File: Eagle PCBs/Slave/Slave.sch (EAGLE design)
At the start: 7 parts, among them Q1 TIP120

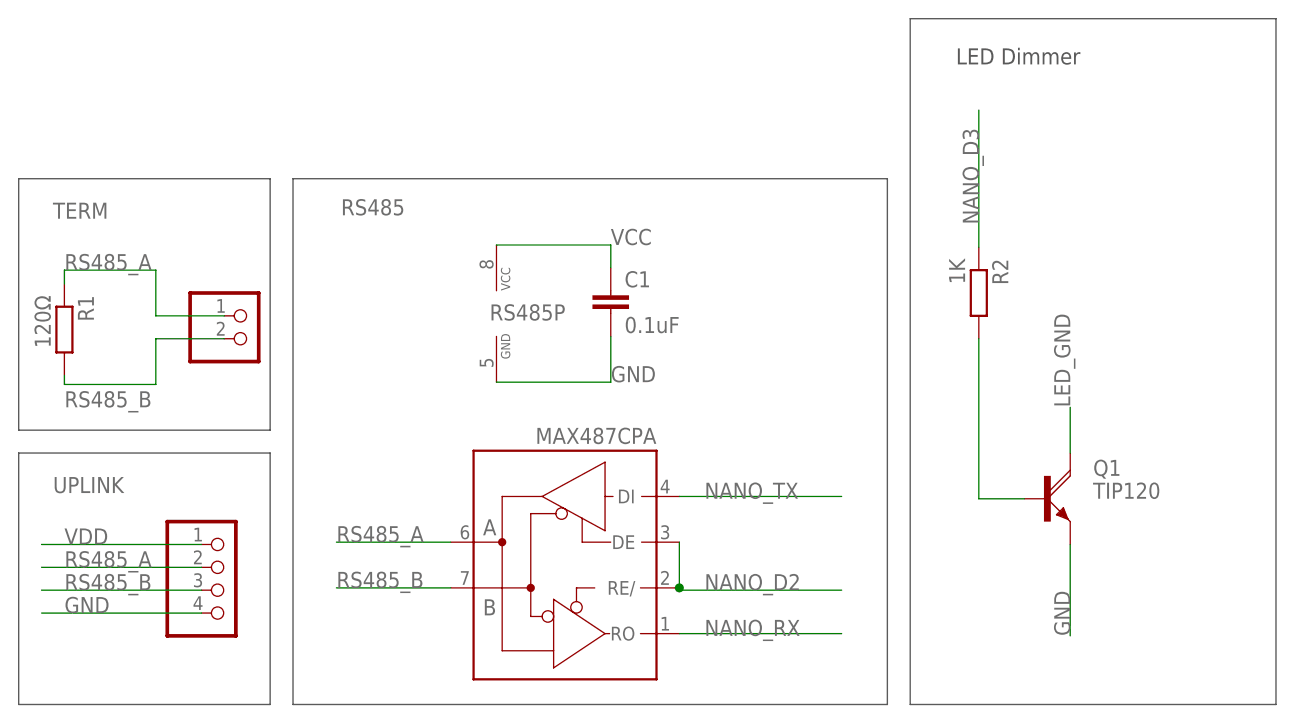
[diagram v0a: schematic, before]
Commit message: Added LED circuit to Slave PCB
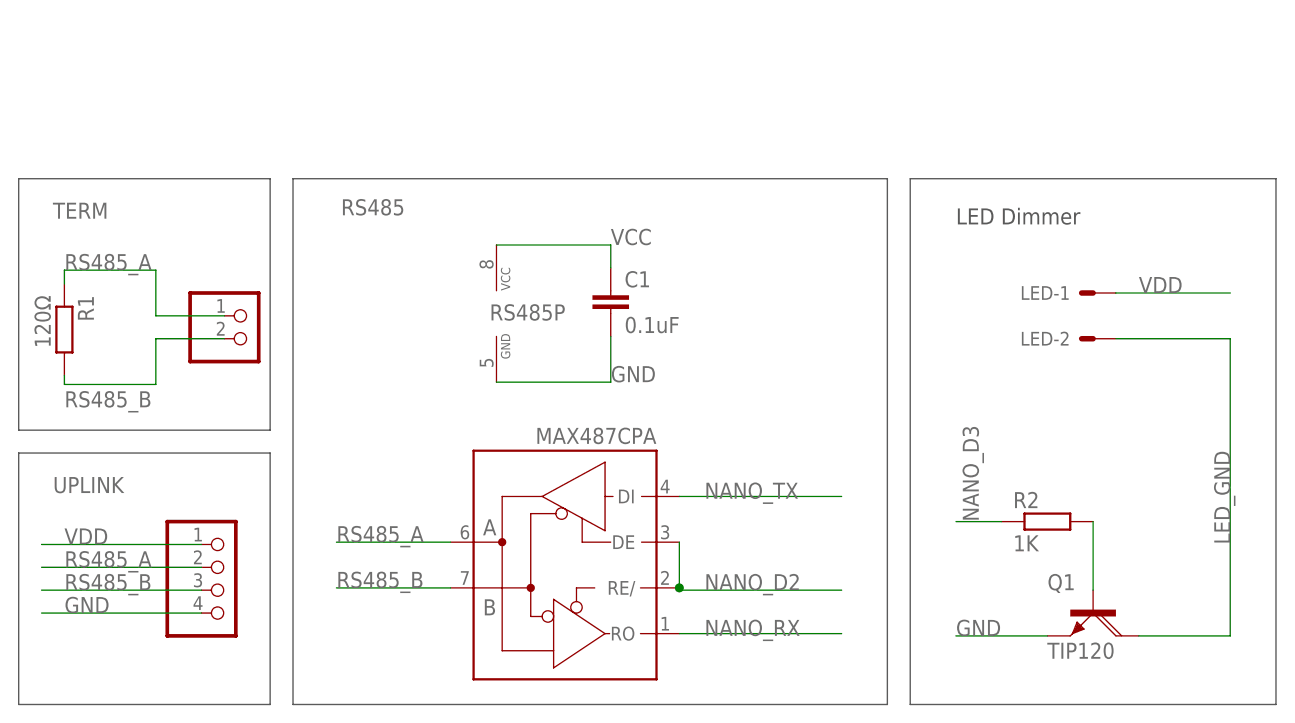
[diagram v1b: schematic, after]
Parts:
- added LED: (no value), con-molex:KK-156-2
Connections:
- net LED_GND: now also LED-2.S
- net VDD: now also LED-1.S
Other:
- moved on the sheet: Q1, R2
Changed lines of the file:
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@@
 <part name="Q1" library="transistor-power" library_urn="urn:adsk.eagle:library:400" deviceset="TIP120" device="" package3d_urn="urn:adsk.eagle:package:29488/1"/>
 <part name="UPLINK" library="pinhead" library_urn="urn:adsk.eagle:library:325" deviceset="PINHD-1X4" device="" package3d_urn="urn:adsk.eagle:package:22407/2"/>
+<part name="LED" library="con-molex" library_urn="urn:adsk.eagle:library:165" deviceset="KK-156-2" device="" package3d_urn="urn:adsk.eagle:package:8078800/1"/>
 </parts>
 <sheets>
 <sheet>
 <plain>
-<text x="106.68" y="73.66" size="1.778" layer="97">LED Dimmer</text>
-<wire x1="101.6" y1="78.74" x2="142.24" y2="78.74" width="0.1524" layer="97"/>
-<wire x1="142.24" y1="78.74" x2="142.24" y2="2.54" width="0.1524" layer="97"/>
+<text x="106.68" y="55.88" size="1.778" layer="97">LED Dimmer</text>
+<wire x1="101.6" y1="60.96" x2="142.24" y2="60.96" width="0.1524" layer="97"/>
+<wire x1="142.24" y1="60.96" x2="142.24" y2="2.54" width="0.1524" layer="97"/>
 <wire x1="142.24" y1="2.54" x2="101.6" y2="2.54" width="0.1524" layer="97"/>
-<wire x1="101.6" y1="2.54" x2="101.6" y2="78.74" width="0.1524" layer="97"/>
+<wire x1="101.6" y1="2.54" x2="101.6" y2="60.96" width="0.1524" layer="97"/>
 <wire x1="2.54" y1="2.54" x2="2.54" y2="30.48" width="0.1524" layer="97"/>
 <wire x1="2.54" y1="30.48" x2="30.48" y2="30.48" width="0.1524" layer="97"/>
@@
 <attribute name="VALUE" x="4.318" y="48.006" size="1.778" layer="96" rot="R270"/>
 </instance>
-<instance part="R2" gate="G$1" x="109.22" y="48.26" smashed="yes" rot="R270">
-<attribute name="NAME" x="110.7186" y="52.07" size="1.778" layer="95" rot="R270"/>
-<attribute name="VALUE" x="105.918" y="52.07" size="1.778" layer="96" rot="R270"/>
+<instance part="R2" gate="G$1" x="116.84" y="22.86" smashed="yes">
+<attribute name="NAME" x="113.03" y="24.3586" size="1.778" layer="95"/>
+<attribute name="VALUE" x="113.03" y="19.558" size="1.778" layer="96"/>
 </instance>
-<instance part="Q1" gate="1" x="116.84" y="25.4" smashed="yes">
-<attribute name="NAME" x="121.92" y="27.94" size="1.778" layer="95"/>
-<attribute name="VALUE" x="121.92" y="25.4" size="1.778" layer="96"/>
+<instance part="Q1" gate="1" x="121.92" y="12.7" smashed="yes" rot="R270">
+<attribute name="NAME" x="116.84" y="15.24" size="1.778" layer="95"/>
+<attribute name="VALUE" x="116.84" y="7.62" size="1.778" layer="96"/>
 </instance>
 <instance part="UPLINK" gate="A" x="25.4" y="15.24" smashed="yes">
 <attribute name="NAME" x="6.35" y="26.035" size="1.778" layer="95"/>
 <attribute name="VALUE" x="19.05" y="7.62" size="1.778" layer="96"/>
+</instance>
+<instance part="LED" gate="-1" x="121.92" y="48.26" smashed="yes" rot="R180">
+<attribute name="NAME" x="119.38" y="49.022" size="1.524" layer="95" rot="R180"/>
+<attribute name="VALUE" x="122.682" y="46.863" size="1.778" layer="96" rot="R180"/>
+</instance>
+<instance part="LED" gate="-2" x="121.92" y="43.18" smashed="yes" rot="R180">
+<attribute name="NAME" x="119.38" y="43.942" size="1.524" layer="95" rot="R180"/>
+<attribute name="VALUE" x="122.682" y="41.783" size="1.778" layer="96" rot="R180"/>
 </instance>
 </instances>
@@
 <label x="7.62" y="20.32" size="1.778" layer="95"/>
 <pinref part="UPLINK" gate="A" pin="1"/>
+</segment>
+<segment>
+<pinref part="LED" gate="-1" pin="S"/>
+<wire x1="124.46" y1="48.26" x2="137.16" y2="48.26" width="0.1524" layer="91"/>
+<label x="127" y="48.26" size="1.778" layer="95"/>
 </segment>
 </net>
@@
 <segment>
 <pinref part="Q1" gate="1" pin="E"/>
-<wire x1="119.38" y1="20.32" x2="119.38" y2="10.16" width="0.1524" layer="91"/>
-<label x="119.38" y="10.16" size="1.778" layer="95" rot="R90"/>
+<wire x1="116.84" y1="10.16" x2="106.68" y2="10.16" width="0.1524" layer="91"/>
+<label x="106.68" y="10.16" size="1.778" layer="95"/>
 </segment>
 </net>
@@
 <segment>
 <pinref part="R2" gate="G$1" pin="2"/>
-<wire x1="109.22" y1="43.18" x2="109.22" y2="25.4" width="0.1524" layer="91"/>
 <pinref part="Q1" gate="1" pin="B"/>
-<wire x1="109.22" y1="25.4" x2="114.3" y2="25.4" width="0.1524" layer="91"/>
+<wire x1="121.92" y1="22.86" x2="121.92" y2="15.24" width="0.1524" layer="91"/>
 </segment>
 </net>
@@
 <segment>
 <pinref part="Q1" gate="1" pin="C"/>
-<wire x1="119.38" y1="30.48" x2="119.38" y2="35.56" width="0.1524" layer="91"/>
-<label x="119.38" y="35.56" size="1.778" layer="95" rot="R90"/>
+<wire x1="127" y1="10.16" x2="137.16" y2="10.16" width="0.1524" layer="91"/>
+<label x="137.16" y="20.32" size="1.778" layer="95" rot="R90"/>
+<pinref part="LED" gate="-2" pin="S"/>
+<wire x1="124.46" y1="43.18" x2="137.16" y2="43.18" width="0.1524" layer="91"/>
+<wire x1="137.16" y1="43.18" x2="137.16" y2="10.16" width="0.1524" layer="91"/>
 </segment>
 </net>
@@
 <segment>
 <pinref part="R2" gate="G$1" pin="1"/>
-<wire x1="109.22" y1="53.34" x2="109.22" y2="68.58" width="0.1524" layer="91"/>
-<label x="109.22" y="55.88" size="1.778" layer="95" rot="R90"/>
+<wire x1="111.76" y1="22.86" x2="106.68" y2="22.86" width="0.1524" layer="91"/>
+<label x="109.22" y="22.86" size="1.778" layer="95" rot="R90"/>
 </segment>
 </net>
